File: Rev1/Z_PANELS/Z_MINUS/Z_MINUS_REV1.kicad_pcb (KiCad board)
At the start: 2 copper layers, 98 x 98 mm, 0 parts

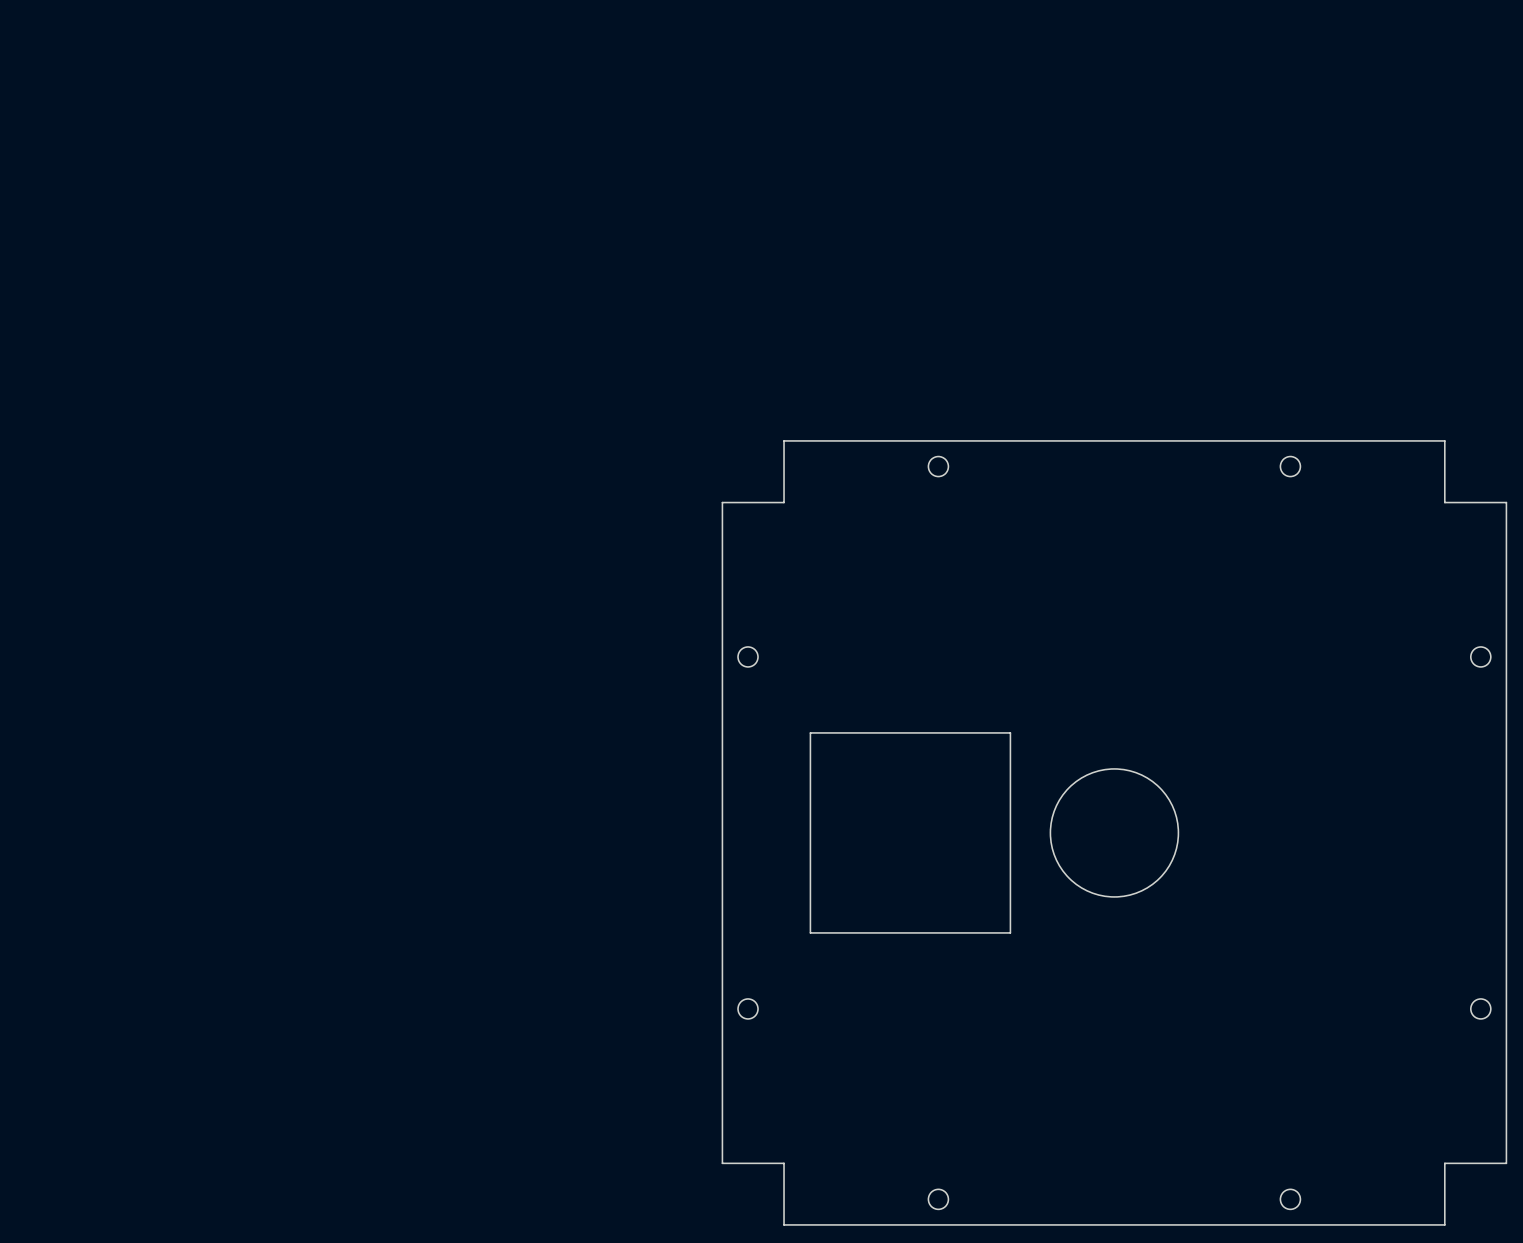
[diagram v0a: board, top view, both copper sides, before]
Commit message: changed resistor sizes;
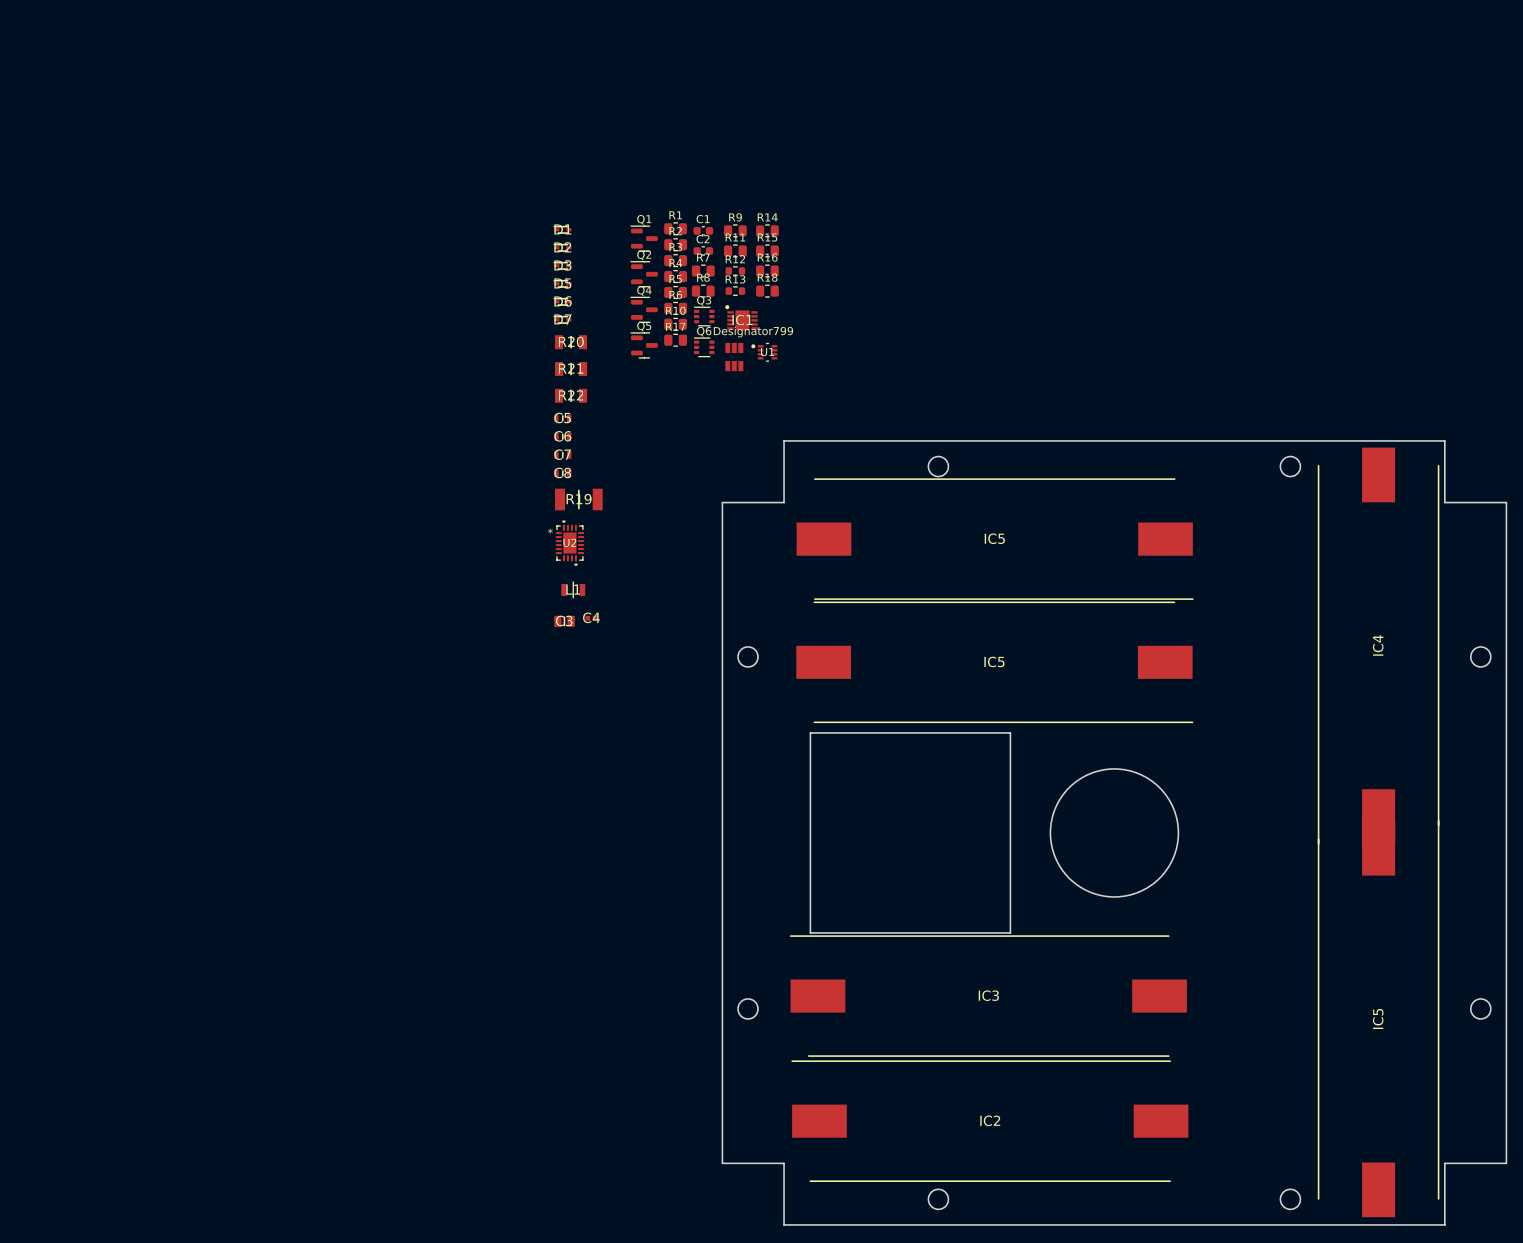
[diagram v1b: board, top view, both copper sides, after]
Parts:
- added C1: 10nF, Capacitor_SMD:C_0603_1608Metric, F.Cu at (85.6, 26.2)
- added C2: 10nF, Capacitor_SMD:C_0603_1608Metric, F.Cu at (85.6, 28.7)
- added C3: CL21A476MQYNNNE, AA_AUTO_LOADER:CAPC2012X135N, F.Cu at (68.2, 75.0)
- added C4: CL05A105KQ5NNNC, AA_AUTO_LOADER:CAPC1005X55N, F.Cu at (71.6, 74.6)
- added C5: CL10A475KQ8NNNC, AA_AUTO_LOADER:CAPC1608X90N, F.Cu at (68.0, 49.6)
- added C6: CGA3E2X7R1H223K080AA, AA_AUTO_LOADER:CAPC1608X90N, F.Cu at (68.0, 51.9)
- added C7: CGA3E2X7R1H223K080AA, AA_AUTO_LOADER:CAPC1608X90N, F.Cu at (68.0, 54.2)
- added C8: CL10A475KQ8NNNC, AA_AUTO_LOADER:CAPC1608X90N, F.Cu at (68.0, 56.5)
- added D1: RB521S30T1G, AA_AUTO_LOADER:SODFL1608X70N, F.Cu at (68.0, 26.0)
- added D2: RB521S30T1G, AA_AUTO_LOADER:SODFL1608X70N, F.Cu at (68.0, 28.3)
- added D3: RB521S30T1G, AA_AUTO_LOADER:SODFL1608X70N, F.Cu at (68.0, 30.5)
- added D5: RB521S30T1G, AA_AUTO_LOADER:SODFL1608X70N, F.Cu at (68.0, 32.8)
- added D6: RB521S30T1G, AA_AUTO_LOADER:SODFL1608X70N, F.Cu at (68.0, 35.0)
- added D7: RB521S30T1G, AA_AUTO_LOADER:SODFL1608X70N, F.Cu at (68.0, 37.3)
- added IC1: LTC4316IDD#PBF, AA_AUTO_LOADER:SON50P300X300X85-11N-D, F.Cu at (90.5, 37.4)
- added IC2: SM141K04TFV, AA_AUTO_LOADER:SODFL490150X120N, F.Cu at (121.4, 137.5)
- added IC3: SM141K04TFV, AA_AUTO_LOADER:SODFL490150X120N, F.Cu at (121.2, 121.8)
- added IC4: SM141K04TFV, AA_AUTO_LOADER:SODFL490150X120N, F.Cu at (170.0, 78.0)
- added IC5: SM141K04TFV, AA_AUTO_LOADER:SODFL490150X120N, F.Cu at (170.0, 124.7)
- added IC5: SM141K04TFV, AA_AUTO_LOADER:SODFL490150X120N, F.Cu at (122.0, 80.1)
- added IC5: SM141K04TFV, AA_AUTO_LOADER:SODFL490150X120N, F.Cu at (122.0, 64.7)
- added JP1: ~, SparkFun-Jumper:SMT-JUMPER_3_NO_NO-SILK, F.Cu at (89.4, 40.8)
- added JP2: ~, SparkFun-Jumper:SMT-JUMPER_3_NO_NO-SILK, F.Cu at (89.4, 43.1)
- added L1: LQM2HPN4R7MG0L, AA_AUTO_LOADER:LQM2HPN1R0MG0L, F.Cu at (69.3, 71.1)
- added Q1: BSS138, Package_TO_SOT_SMD:SOT-23, F.Cu at (78.2, 27.1)
- added Q2: BSS138, Package_TO_SOT_SMD:SOT-23, F.Cu at (78.2, 31.6)
- added Q3: MBT2222ADW1T1, Package_TO_SOT_SMD:SOT-363_SC-70-6, F.Cu at (85.7, 36.9)
- added Q4: BSS138, Package_TO_SOT_SMD:SOT-23, F.Cu at (78.2, 36.0)
- added Q5: BSS138, Package_TO_SOT_SMD:SOT-23, F.Cu at (78.2, 40.5)
- added Q6: MBT2222ADW1T1, Package_TO_SOT_SMD:SOT-363_SC-70-6, F.Cu at (85.7, 40.7)
- added R1: 280k, Resistor_SMD:R_0805_2012Metric, F.Cu at (82.1, 25.9)
- added R10: 10K, Resistor_SMD:R_0805_2012Metric, F.Cu at (82.1, 37.9)
- added R11: 100K, Resistor_SMD:R_0805_2012Metric, F.Cu at (89.6, 28.7)
- added R12: 0, Resistor_SMD:R_0603_1608Metric, F.Cu at (89.6, 31.2)
- added R13: 0, Resistor_SMD:R_0603_1608Metric, F.Cu at (89.6, 33.7)
- added R14: 10K, Resistor_SMD:R_0805_2012Metric, F.Cu at (93.6, 26.2)
- added R15: 600, Resistor_SMD:R_0805_2012Metric, F.Cu at (93.6, 28.7)
- added R16: 10K, Resistor_SMD:R_0805_2012Metric, F.Cu at (93.6, 31.2)
- added R17: 10K, Resistor_SMD:R_0805_2012Metric, F.Cu at (82.1, 39.8)
- added R18: 100K, Resistor_SMD:R_0805_2012Metric, F.Cu at (93.6, 33.7)
- added R19: CHV2010-FX-1005ELF, AA_AUTO_LOADER:RESC5025X70N, F.Cu at (70.0, 59.8)
- added R2: 1000k, Resistor_SMD:R_0805_2012Metric, F.Cu at (82.1, 27.9)
- added R20: RC1206FR-072M49L, AA_AUTO_LOADER:RESC3116X65N, F.Cu at (69.0, 40.1)
- added R21: RV1206JR-0722ML, AA_AUTO_LOADER:RESC3116X65N, F.Cu at (69.0, 43.4)
- added R22: RC1206FR-072ML, AA_AUTO_LOADER:RESC3116X65N, F.Cu at (69.0, 46.8)
- added R3: 10K, Resistor_SMD:R_0805_2012Metric, F.Cu at (82.1, 29.9)
- added R4: 10K, Resistor_SMD:R_0805_2012Metric, F.Cu at (82.1, 31.9)
- added R5: 10K, Resistor_SMD:R_0805_2012Metric, F.Cu at (82.1, 33.9)
- added R6: 10K, Resistor_SMD:R_0805_2012Metric, F.Cu at (82.1, 35.9)
- added R7: 10K, Resistor_SMD:R_0805_2012Metric, F.Cu at (85.6, 31.2)
- added R8: 600, Resistor_SMD:R_0805_2012Metric, F.Cu at (85.6, 33.7)
- added R9: 10K, Resistor_SMD:R_0805_2012Metric, F.Cu at (89.6, 26.2)
- added U1: OPT4001DTST, OPT4001DTST:DTS0008A-MFG, F.Cu at (93.6, 41.4)
- added U2: LTC3130EUDC-1-PBF, LTC3130:UDC_20_ADI, F.Cu at (68.9, 65.2)

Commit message: made changes to Z minus and Z plus cutouts
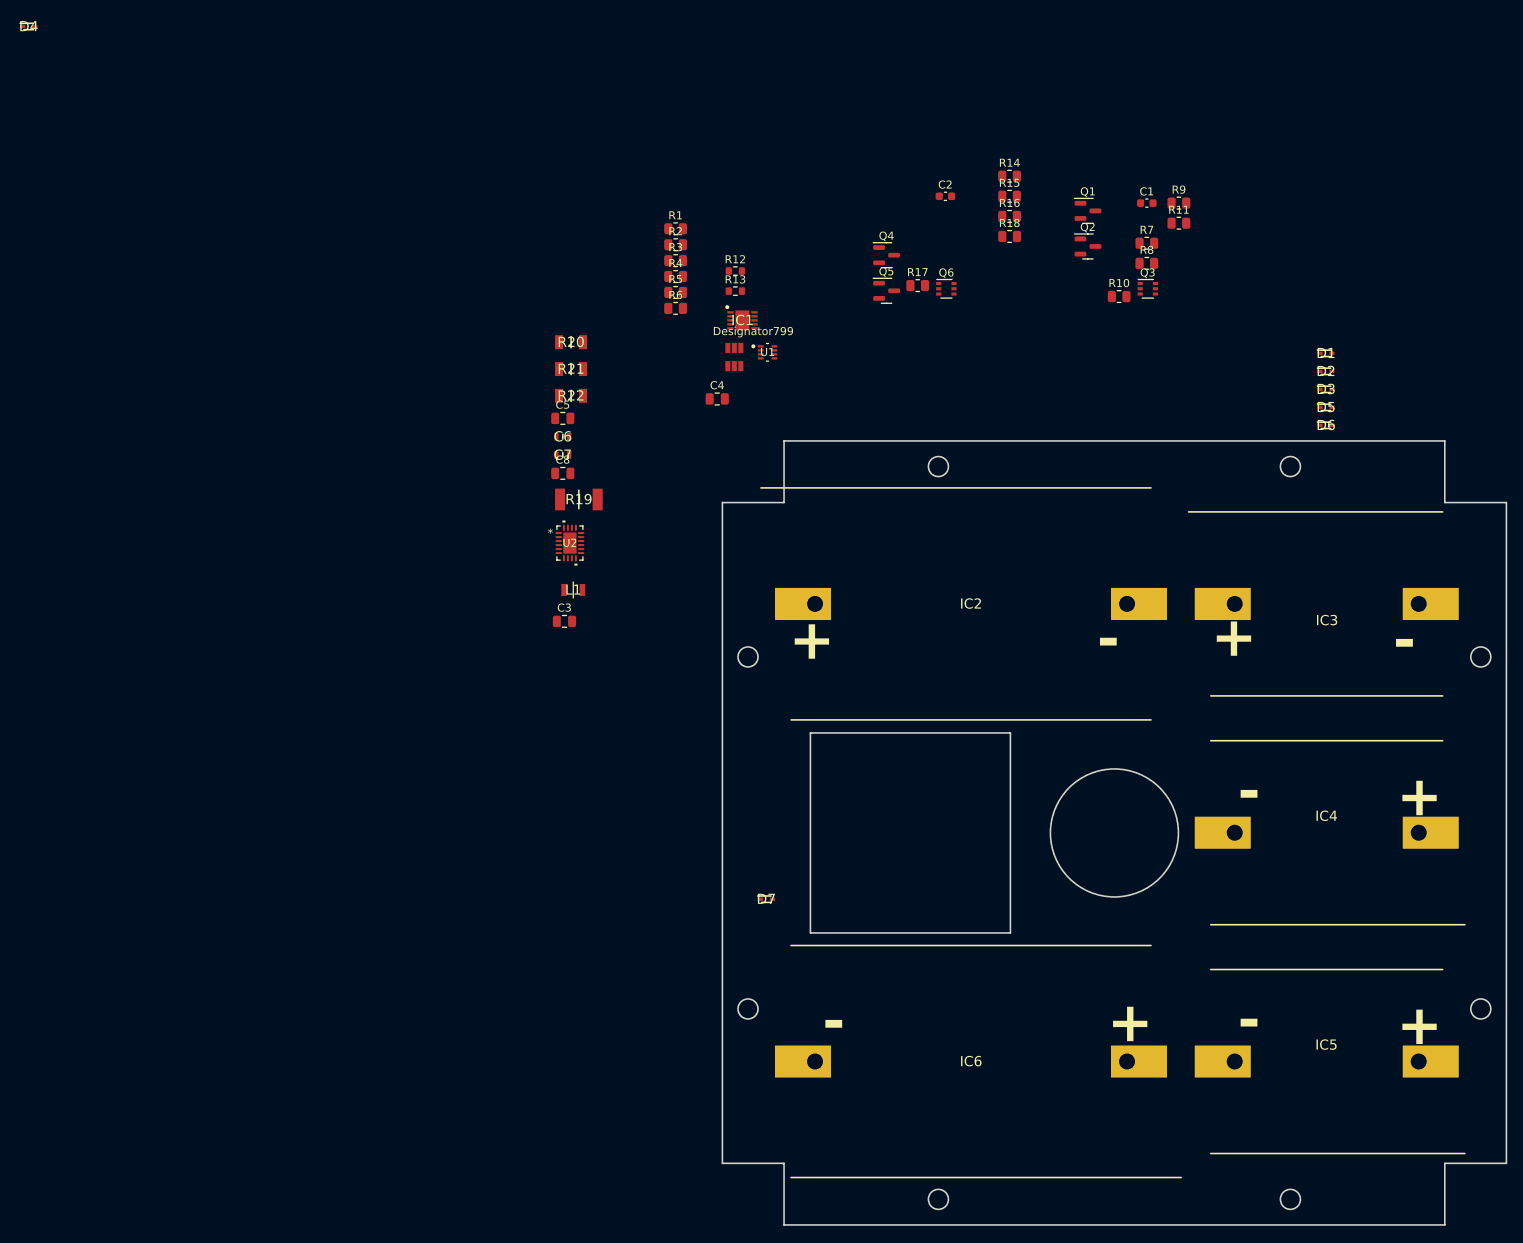
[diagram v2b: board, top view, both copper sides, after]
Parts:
- removed the IC5 at (170.0, 124.7)
- removed the IC5 at (122.0, 80.1)
- removed the IC5 at (122.0, 64.7)
- added D4: RB521S30T1G, AA_AUTO_LOADER:SODFL1608X70N, F.Cu at (1.25, 0.62)
- added IC5: SM141K04TFV, AA_AUTO_LOADER:SODFL340230X120N, F.Cu at (163.5, 130.0)
- added IC6: SM141K08TFV, AA_AUTO_LOADER:SODFL520290X120N, F.Cu at (119.0, 130.0)
- C3: value CL21A476MQYNNNE -> 47uF; footprint AA_AUTO_LOADER:CAPC2012X135N -> Capacitor_SMD:C_0805_2012Metric
- C4: value CL05A105KQ5NNNC -> 1uF; footprint AA_AUTO_LOADER:CAPC1005X55N -> Capacitor_SMD:C_0805_2012Metric
- C5, C8: value CL10A475KQ8NNNC -> 4.7uF; footprint AA_AUTO_LOADER:CAPC1608X90N -> Capacitor_SMD:C_0805_2012Metric
- IC2: value SM141K04TFV -> SM141K08TFV; footprint AA_AUTO_LOADER:SODFL490150X120N -> AA_AUTO_LOADER:SODFL520290X120N
- IC3, IC4: footprint AA_AUTO_LOADER:SODFL490150X120N -> AA_AUTO_LOADER:SODFL340230X120N
- moved D1 96.6 mm to (163.4, 41.5)
- moved D2 96.6 mm to (163.4, 43.7)
- moved D3 96.6 mm to (163.4, 46.0)
- moved D5 96.6 mm to (163.4, 48.2)
- moved D6 96.6 mm to (163.4, 50.5)
- moved D7 76.8 mm to (93.5, 109.7)
- moved IC3 64.7 mm to (163.5, 72.8)
- moved IC2 64.7 mm to (119.0, 72.8)
- moved Q1 55.5 mm to (133.7, 23.7)
- moved Q2 55.5 mm to (133.7, 28.1)
- moved R10 55.5 mm to (137.6, 34.4)
- moved R11 55.5 mm to (145.0, 25.2)
- moved R9 55.5 mm to (145.0, 22.7)
- moved C1 55.5 mm to (141.0, 22.7)
- moved Q3 55.5 mm to (141.1, 33.4)
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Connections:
- C3 pad 1: GND -> Net-(U2-PVIN)
- C3 pad 2: Net-(U2-PVIN) -> GND
- C4 pad 1: GND -> Net-(U2-PVIN)
- C4 pad 2: Net-(U2-PVIN) -> GND
- C5 pad 1: GND -> Net-(U2-VCC)
- C5 pad 2: Net-(U2-VCC) -> GND
- C8 pad 1: GND -> Net-(U2-VOUT)
- C8 pad 2: Net-(U2-VOUT) -> GND
- D1 pad 1: Net-(IC2-NEG) -> /SOLAR_PANEL_ELECTRONICS/7023_vout
- D1 pad 2: Net-(IC3-NEG) -> Net-(IC2-NEG)
- D2 pad 1: VSOLAR -> Net-(IC2-NEG)
- D2 pad 2: Net-(U2-VOUT) -> unconnected-(D2-Pad2)
- D3 pad 1: /SOLAR_PANEL_ELECTRONICS/7023_vout -> Net-(IC3-NEG)
- D3 pad 2: Net-(IC2-NEG) -> Net-(IC4-NEG)
- D5 pad 1: Net-(IC3-NEG) -> Net-(IC4-NEG)
- D5 pad 2: Net-(IC4-NEG) -> Net-(IC5-NEG)
- D6 pad 1: Net-(IC4-NEG) -> Net-(IC5-NEG)
- D7 pad 1: Net-(U2-PVIN) -> VSOLAR
- D7 pad 2: /SOLAR_PANEL_ELECTRONICS/7023_vout -> Net-(U2-VOUT)
